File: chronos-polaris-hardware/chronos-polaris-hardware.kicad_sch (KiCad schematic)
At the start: 61 parts, among them J1 Conn_01x03_Pin, J2 Conn_01x03_Pin, J3 Conn_01x03_Pin, J4 Conn_01x03_Pin, J5 Conn_01x03_Pin, J6 Conn_01x04, J7 Conn_01x04, J8 Conn_01x02, P1 WJ124-3_81-6P, U1 TPS62172DSGR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

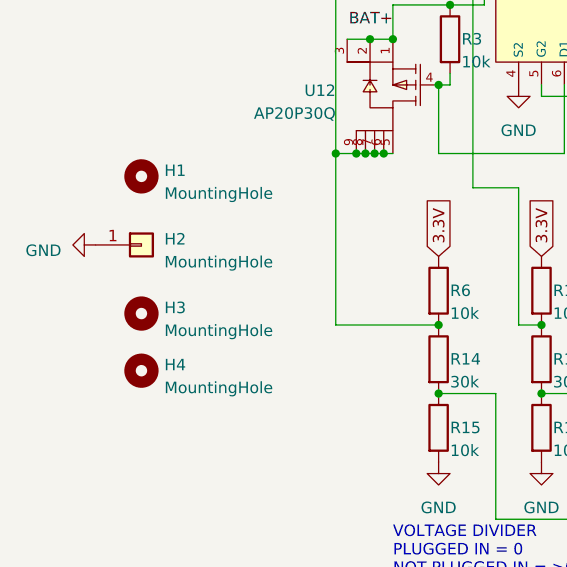
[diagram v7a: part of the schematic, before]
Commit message: polaris routing with fix V
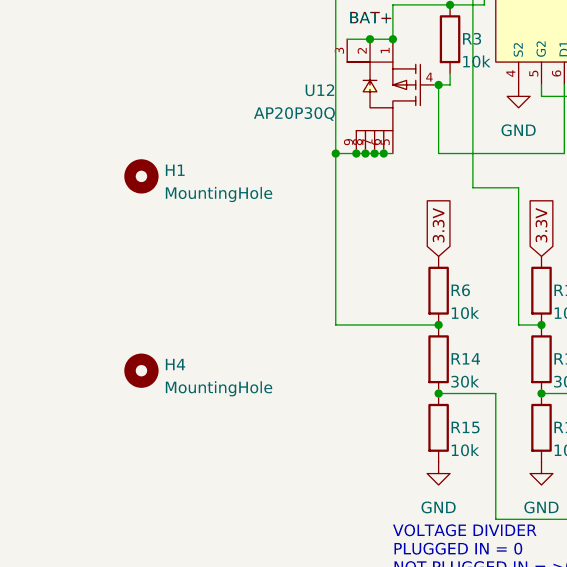
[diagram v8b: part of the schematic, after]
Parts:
- removed H2: MountingHole, MountingHole:MountingHole_3.2mm_M3_Pad, symbol Connector_Generic:Conn_01x01
- removed H3: MountingHole, MountingHole:MountingHole_3.2mm_M3_Pad, symbol Mechanical:MountingHole
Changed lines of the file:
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@@
-    )
-  )
-  (symbol (lib_id "power:GND") (at 30.48 135.89 270) (unit 1)
-    (in_bom yes) (on_board yes) (dnp no) (fields_autoplaced)
-    (property "Reference" "#PWR050" (at 24.13 135.89 0)
-      (effects (font (size 1.27 1.27)) hide)
-    )
-    (property "Value" "GND" (at 26.67 136.525 90)
-      (effects (font (size 1.27 1.27)) (justify right))
-    )
-    (property "Footprint" "" (at 30.48 135.89 0)
-      (effects (font (size 1.27 1.27)) hide)
-    )
-    (property "Datasheet" "" (at 30.48 135.89 0)
-      (effects (font (size 1.27 1.27)) hide)
-    )
-    (pin "1")
-    (instances
-      (project "chronos-polaris-hardware"
-        (path "/503f01d5-a0c6-4ade-b485-97c3c2e1d6c5"
-          (reference "#PWR050") (unit 1)
-        )
-      )
     )
   )
@@
         (path "/503f01d5-a0c6-4ade-b485-97c3c2e1d6c5"
           (reference "R13") (unit 1)
-        )
-      )
-    )
-  )
-  (symbol (lib_id "Mechanical:MountingHole") (at 35.56 143.51 0) (unit 1)
-    (in_bom yes) (on_board yes) (dnp no) (fields_autoplaced)
-    (property "Reference" "H3" (at 38.1 142.875 0)
-      (effects (font (size 1.27 1.27)) (justify left))
-    )
-    (property "Value" "MountingHole" (at 38.1 145.415 0)
-      (effects (font (size 1.27 1.27)) (justify left))
-    )
-    (property "Footprint" "MountingHole:MountingHole_3.2mm_M3_Pad" (at 35.56 143.51 0)
-      (effects (font (size 1.27 1.27)) hide)
-    )
-    (property "Datasheet" "~" (at 35.56 143.51 0)
-      (effects (font (size 1.27 1.27)) hide)
-    )
-    (instances
-      (project "chronos-polaris-hardware"
-        (path "/503f01d5-a0c6-4ade-b485-97c3c2e1d6c5"
-          (reference "H3") (unit 1)
         )
       )
@@
         )
       )
-    )
-  )
-  (symbol (lib_id "Connector_Generic:Conn_01x01") (at 35.56 135.89 0) (unit 1)
-    (in_bom yes) (on_board yes) (dnp no)
-    (property "Reference" "H2" (at 38.1 135.255 0)
-      (effects (font (size 1.27 1.27)) (justify left))
-    )
-    (property "Value" "MountingHole" (at 38.1 137.795 0)
-      (effects (font (size 1.27 1.27)) (justify left))
-    )
-    (property "Footprint" "MountingHole:MountingHole_3.2mm_M3_Pad" (at 35.56 135.89 0)
-      (effects (font (size 1.27 1.27)) hide)
-    )
-    (property "Datasheet" "~" (at 35.56 135.89 0)
-      (effects (font (size 1.27 1.27)) hide)
-    )
-    (pin "1")
-    (instances
-      (project "chronos-polaris-hardware"
-        (path "/503f01d5-a0c6-4ade-b485-97c3c2e1d6c5"
-          (reference "H2") (unit 1)
-        )
-      )
